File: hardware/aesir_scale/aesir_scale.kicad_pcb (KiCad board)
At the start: 2 copper layers, 60 x 50 mm, 50 parts, among them J1 jst xh 4, J2 jst gh, J3 jst xh 4, J4 jst_sh 6, J5 jst gh, J6 USB_C_Receptacle_USB2.0, U1 STM32U575CGTx, U2 NAU7802SGI, U3 AZ1117CH2-3.3TRG1, U4 TJA1051T, Y1 48MHz

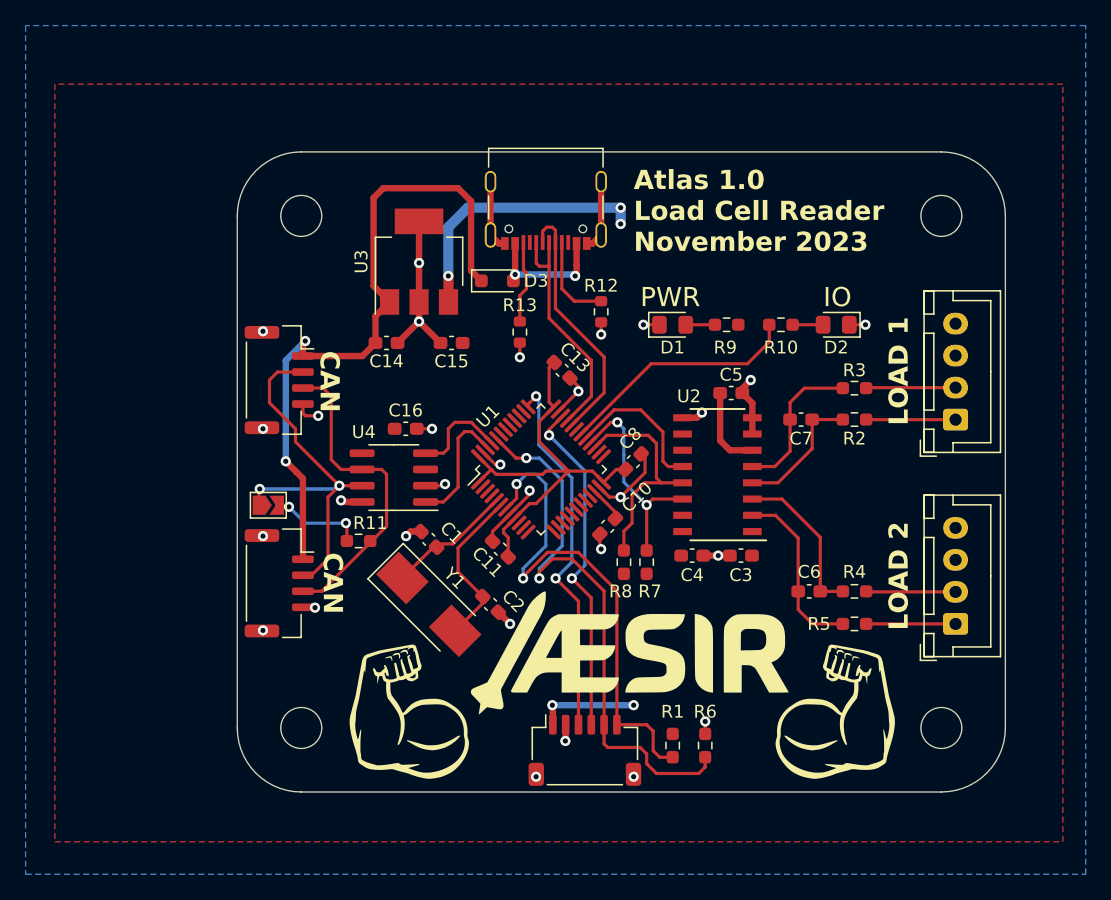
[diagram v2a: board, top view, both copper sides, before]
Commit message: correct i2c bus
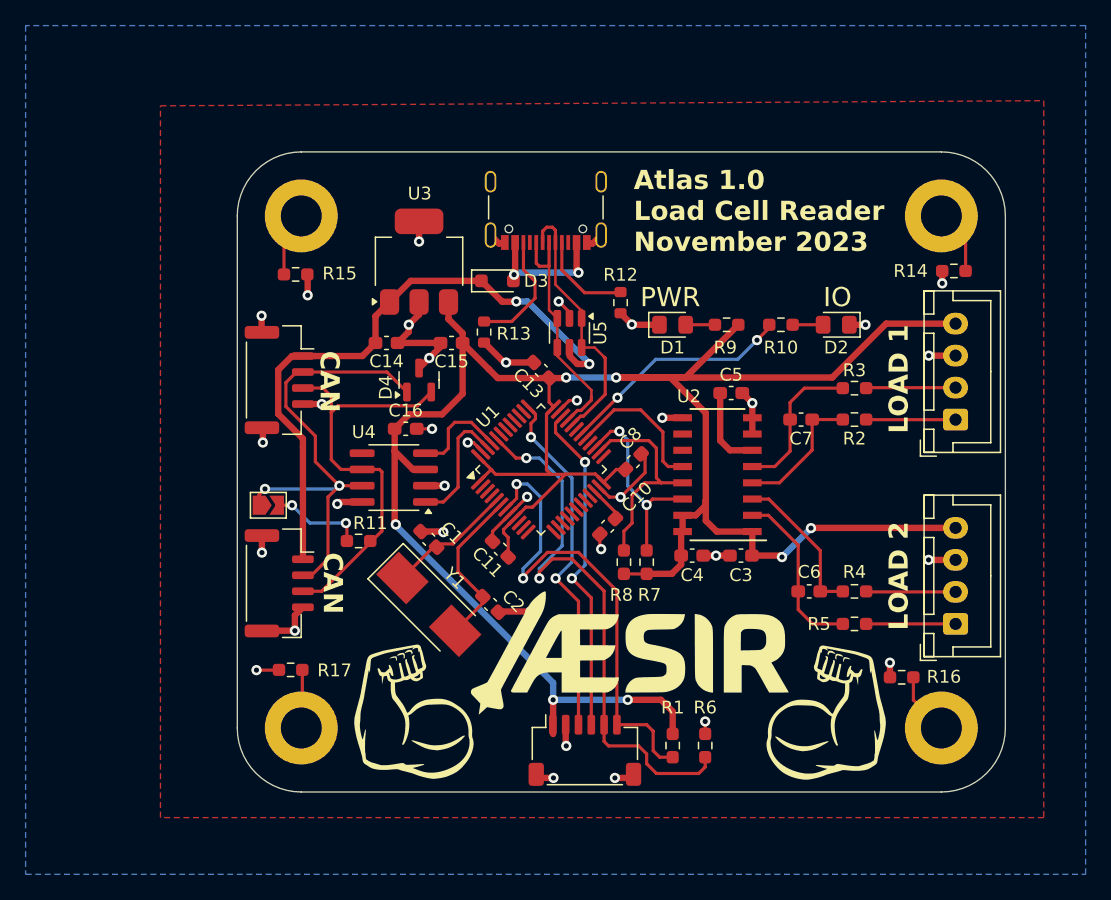
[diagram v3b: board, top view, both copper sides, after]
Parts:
- added D4: NUP2105L, Package_TO_SOT_SMD:SOT-23, F.Cu at (76.2, 83.8)
- added R14: 1M, Resistor_SMD:R_0603_1608Metric_Pad0.98x0.95mm_HandSolder, F.Cu at (118.0, 75.3)
- added R15: 1M, Resistor_SMD:R_0603_1608Metric_Pad0.98x0.95mm_HandSolder, F.Cu at (66.6, 75.6)
- added R16: 1M, Resistor_SMD:R_0603_1608Metric_Pad0.98x0.95mm_HandSolder, F.Cu at (113.9, 107.0)
- added R17: 1M, Resistor_SMD:R_0603_1608Metric_Pad0.98x0.95mm_HandSolder, F.Cu at (66.2, 106.5)
- added U5: USBLC6-2SC6, Package_TO_SOT_SMD:SOT-23-6, F.Cu at (88.0, 80.1)
- C14: value 22u -> 10u
- C15: value 10u -> 22u
- C5: value 0u1 -> 100n
- H1, H2, H3, H4: footprint MountingHole:MountingHole_3.2mm_M3_ISO7380 -> MountingHole:MountingHole_3.2mm_M3_ISO7380_Pad
- R10, R9: value 500 -> 470
- moved R13 2.79 mm to (81.3, 80.1)
- moved R12 1.67 mm to (91.9, 77.8)
- moved C13 1.63 mm to (85.8, 83.1), turned to 135 degrees
- moved G*** 0.72 mm to (108.0, 109.8)
- moved G*** 0.36 mm to (75.8, 109.7)
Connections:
- U1 pad 26: unconnected-(U1-PB13-Pad26) -> /SCL
- U1 pad 27: /SCL -> /SDA
- U1 pad 28: /SDA -> unconnected-(U1-PB15-Pad28)
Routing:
- net +3V3: track 63.0 -> 195.6 mm, vias 5 -> 7
- net Earth: track 67.9 -> 82.4 mm, vias 29 -> 35
- net /CAN_L: track 24.9 -> 33.0 mm
- net /CAN_H: track 31.4 -> 38.0 mm
- net Net-(H2-Pad1): track 0.00 -> 5.13 mm
- net Net-(H1-Pad1): track 0.00 -> 5.08 mm
- net Net-(H3-Pad1): track 0.00 -> 4.87 mm
- net Net-(H4-Pad1): track 0.00 -> 4.57 mm
- net VCC: track 53.3 -> 49.8 mm
- net Net-(J6-CC2): track 6.06 -> 9.46 mm
- net /USB_D_N: track 19.5 -> 21.4 mm
- net /NRST: track 39.9 -> 38.1 mm
- net /SW_CLK: track 29.4 -> 28.1 mm
- net /SDA: track 16.8 -> 15.7 mm
- net /SCL: track 17.6 -> 16.9 mm
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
